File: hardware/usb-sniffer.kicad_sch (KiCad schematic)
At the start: 40 parts, among them IC1 LCMXO2-2000HC-5TG100, IC2 MIC5504-3.3v, J1 USB-C, J2 USB-C, J3 USB-A, J4 IN, J5 GND

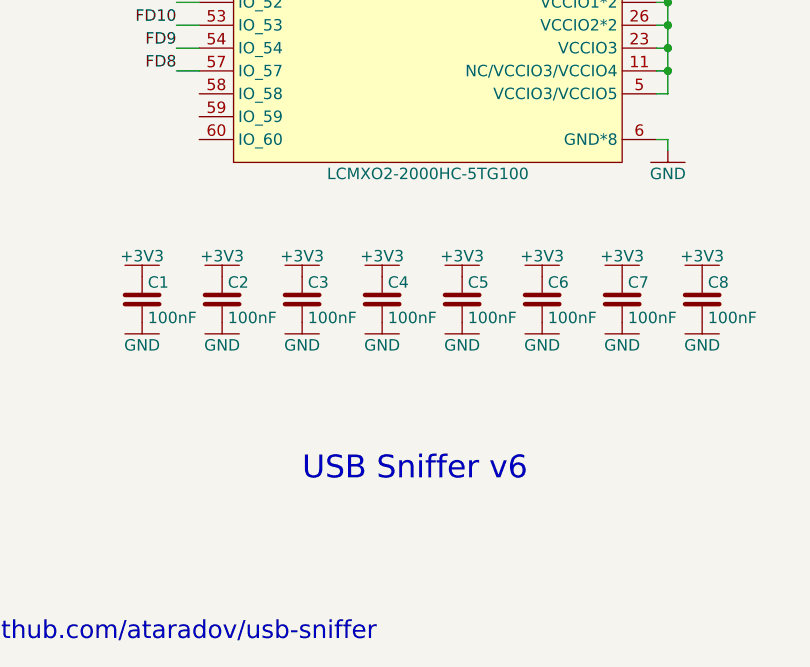
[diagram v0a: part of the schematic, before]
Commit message: replace obsolete components, updated PCB, schematics and production files
Signed-off-by: Jakub Sobota <jakub.sobota@3mdeb.com>
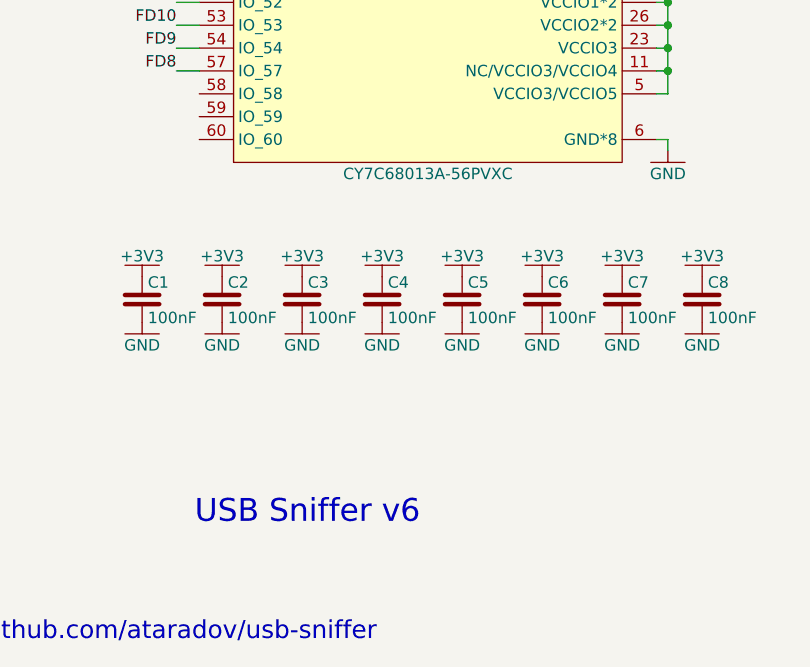
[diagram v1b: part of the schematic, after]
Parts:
- IC1: value LCMXO2-2000HC-5TG100 -> CY7C68013A-56PVXC
- TP1, TP2, TP3, TP4, TP5, TP6, TP7, TP8: value (none) -> ~
